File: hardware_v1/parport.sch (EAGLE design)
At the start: 13 parts, among them IC1 74LS541DW, IC2 74LS541DW, IC3 74LS541DW, K1 PIN20X2

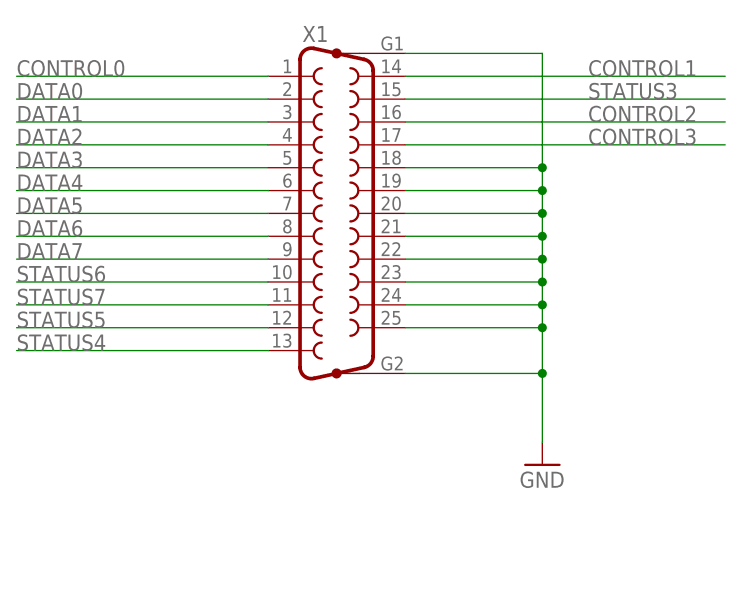
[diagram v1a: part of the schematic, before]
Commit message: hardware_v1: replace DB25 with 2x13 header
It was a mistake to mount a DB25 directly on the adapter.
Use a 26 pin header and then off the shelf header to DB25
adapters can be used to suit the application.
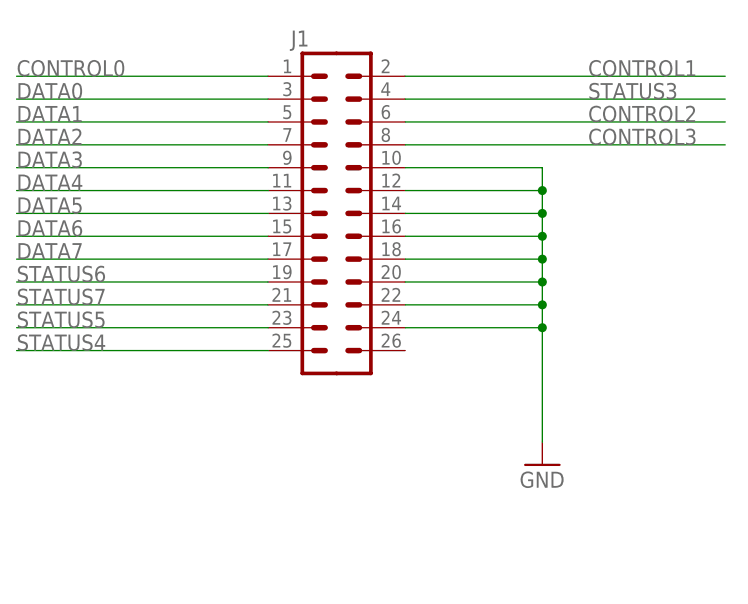
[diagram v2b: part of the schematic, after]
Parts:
- removed X1: (no value), con-subd:F25HP
- added J1: (no value), SparkFun-Connectors:M13X22X13
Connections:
- net CONTROL0: now also J1.1; no longer X1.1
- net CONTROL1: now also J1.2; no longer X1.14
- net CONTROL2: now also J1.6; no longer X1.16
- net CONTROL3: now also J1.8; no longer X1.17
- net DATA0: now also J1.3; no longer X1.2
- net DATA1: now also J1.5; no longer X1.3
- net DATA2: now also J1.7; no longer X1.4
- net DATA3: now also J1.9; no longer X1.5
- net DATA4: now also J1.11; no longer X1.6
- net DATA5: now also J1.13; no longer X1.7
- net DATA6: now also J1.15; no longer X1.8
- net DATA7: now also J1.17; no longer X1.9
- net GND: now also J1.10, J1.12, J1.14, J1.16, J1.18, J1.20, J1.22, J1.24; no longer X1.18, X1.19, X1.20, X1.21, X1.22, X1.23, X1.24, X1.25, X1.G1, X1.G2
- net STATUS3: now also J1.4; no longer X1.15
- net STATUS4: now also J1.25; no longer X1.13
- net STATUS5: now also J1.23; no longer X1.12
- net STATUS6: now also J1.19; no longer X1.10
- net STATUS7: now also J1.21; no longer X1.11
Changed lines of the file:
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@@
 <part name="P+1" library="supply1" deviceset="+5V" device=""/>
 <part name="IC1" library="74xx-us" deviceset="74*541" device="DW" technology="LS"/>
-<part name="X1" library="con-subd" deviceset="F25HP" device=""/>
 <part name="GND1" library="supply1" deviceset="GND" device=""/>
 <part name="IC2" library="74xx-us" deviceset="74*541" device="DW" technology="LS"/>
@@
 <part name="+3V3" library="supply1" deviceset="+3V3" device=""/>
 <part name="P+6" library="supply1" deviceset="+5V" device=""/>
+<part name="J1" library="SparkFun-Connectors" deviceset="M13X2" device="2X13"/>
 </parts>
 <sheets>
@@
 <attribute name="NAME" x="119.38" y="216.535" size="1.778" layer="95"/>
 </instance>
-<instance part="X1" gate="G$1" x="289.56" y="198.12"/>
 <instance part="GND1" gate="1" x="312.42" y="170.18"/>
 <instance part="IC2" gate="A" x="127" y="147.32" smashed="yes">
@@
 <attribute name="VALUE" x="71.12" y="180.34" size="1.778" layer="96" rot="R180"/>
 </instance>
+<instance part="J1" gate="G$1" x="289.56" y="198.12"/>
 </instances>
 <busses>
@@
 </segment>
 <segment>
-<pinref part="X1" gate="G$1" pin="18"/>
 <wire x1="297.18" y1="203.2" x2="312.42" y2="203.2" width="0.1524" layer="91"/>
 <wire x1="312.42" y1="203.2" x2="312.42" y2="200.66" width="0.1524" layer="91"/>
-<pinref part="X1" gate="G$1" pin="19"/>
 <wire x1="312.42" y1="200.66" x2="312.42" y2="198.12" width="0.1524" layer="91"/>
 <wire x1="312.42" y1="198.12" x2="312.42" y2="195.58" width="0.1524" layer="91"/>
@@
 <wire x1="312.42" y1="190.5" x2="312.42" y2="187.96" width="0.1524" layer="91"/>
 <wire x1="312.42" y1="187.96" x2="312.42" y2="185.42" width="0.1524" layer="91"/>
-<wire x1="312.42" y1="185.42" x2="312.42" y2="180.34" width="0.1524" layer="91"/>
-<wire x1="312.42" y1="180.34" x2="312.42" y2="172.72" width="0.1524" layer="91"/>
+<wire x1="312.42" y1="185.42" x2="312.42" y2="172.72" width="0.1524" layer="91"/>
 <wire x1="297.18" y1="200.66" x2="312.42" y2="200.66" width="0.1524" layer="91"/>
 <junction x="312.42" y="200.66"/>
-<pinref part="X1" gate="G$1" pin="20"/>
 <wire x1="297.18" y1="198.12" x2="312.42" y2="198.12" width="0.1524" layer="91"/>
 <junction x="312.42" y="198.12"/>
-<pinref part="X1" gate="G$1" pin="21"/>
 <wire x1="297.18" y1="195.58" x2="312.42" y2="195.58" width="0.1524" layer="91"/>
 <junction x="312.42" y="195.58"/>
-<pinref part="X1" gate="G$1" pin="22"/>
 <wire x1="297.18" y1="193.04" x2="312.42" y2="193.04" width="0.1524" layer="91"/>
 <junction x="312.42" y="193.04"/>
-<pinref part="X1" gate="G$1" pin="23"/>
 <wire x1="297.18" y1="190.5" x2="312.42" y2="190.5" width="0.1524" layer="91"/>
 <junction x="312.42" y="190.5"/>
-<pinref part="X1" gate="G$1" pin="24"/>
 <wire x1="297.18" y1="187.96" x2="312.42" y2="187.96" width="0.1524" layer="91"/>
 <junction x="312.42" y="187.96"/>
-<pinref part="X1" gate="G$1" pin="25"/>
 <wire x1="297.18" y1="185.42" x2="312.42" y2="185.42" width="0.1524" layer="91"/>
 <junction x="312.42" y="185.42"/>
 <pinref part="GND1" gate="1" pin="GND"/>
-<pinref part="X1" gate="G$1" pin="G2"/>
-<wire x1="297.18" y1="180.34" x2="312.42" y2="180.34" width="0.1524" layer="91"/>
-<junction x="312.42" y="180.34"/>
-<pinref part="X1" gate="G$1" pin="G1"/>
-<wire x1="297.18" y1="215.9" x2="312.42" y2="215.9" width="0.1524" layer="91"/>
-<wire x1="312.42" y1="215.9" x2="312.42" y2="203.2" width="0.1524" layer="91"/>
-<junction x="312.42" y="203.2"/>
+<pinref part="J1" gate="G$1" pin="24"/>
+<pinref part="J1" gate="G$1" pin="22"/>
+<pinref part="J1" gate="G$1" pin="20"/>
+<pinref part="J1" gate="G$1" pin="18"/>
+<pinref part="J1" gate="G$1" pin="16"/>
+<pinref part="J1" gate="G$1" pin="14"/>
+<pinref part="J1" gate="G$1" pin="12"/>
+<pinref part="J1" gate="G$1" pin="10"/>
 </segment>
 <segment>
@@
 <net name="DATA0" class="0">
 <segment>
-<pinref part="X1" gate="G$1" pin="2"/>
 <wire x1="281.94" y1="210.82" x2="254" y2="210.82" width="0.1524" layer="91"/>
 <label x="254" y="210.82" size="1.778" layer="95"/>
+<pinref part="J1" gate="G$1" pin="3"/>
 </segment>
 <segment>
@@
 <net name="DATA1" class="0">
 <segment>
-<pinref part="X1" gate="G$1" pin="3"/>
 <wire x1="281.94" y1="208.28" x2="254" y2="208.28" width="0.1524" layer="91"/>
 <label x="254" y="208.28" size="1.778" layer="95"/>
+<pinref part="J1" gate="G$1" pin="5"/>
 </segment>
 <segment>
@@
 <net name="DATA2" class="0">
 <segment>
-<pinref part="X1" gate="G$1" pin="4"/>
 <wire x1="281.94" y1="205.74" x2="254" y2="205.74" width="0.1524" layer="91"/>
 <label x="254" y="205.74" size="1.778" layer="95"/>
+<pinref part="J1" gate="G$1" pin="7"/>
 </segment>
 <segment>
@@
 <net name="DATA3" class="0">
 <segment>
-<pinref part="X1" gate="G$1" pin="5"/>
 <wire x1="281.94" y1="203.2" x2="254" y2="203.2" width="0.1524" layer="91"/>
 <label x="254" y="203.2" size="1.778" layer="95"/>
+<pinref part="J1" gate="G$1" pin="9"/>
 </segment>
 <segment>
@@
 <net name="DATA4" class="0">
 <segment>
-<pinref part="X1" gate="G$1" pin="6"/>
 <wire x1="281.94" y1="200.66" x2="254" y2="200.66" width="0.1524" layer="91"/>
 <label x="254" y="200.66" size="1.778" layer="95"/>
+<pinref part="J1" gate="G$1" pin="11"/>
 </segment>
 <segment>
@@
 <net name="DATA5" class="0">
 <segment>
-<pinref part="X1" gate="G$1" pin="7"/>
 <wire x1="281.94" y1="198.12" x2="254" y2="198.12" width="0.1524" layer="91"/>
 <label x="254" y="198.12" size="1.778" layer="95"/>
+<pinref part="J1" gate="G$1" pin="13"/>
 </segment>
 <segment>
@@
 <net name="DATA6" class="0">
 <segment>
-<pinref part="X1" gate="G$1" pin="8"/>
 <wire x1="281.94" y1="195.58" x2="254" y2="195.58" width="0.1524" layer="91"/>
 <label x="254" y="195.58" size="1.778" layer="95"/>
+<pinref part="J1" gate="G$1" pin="15"/>
 </segment>
 <segment>
@@
 <net name="DATA7" class="0">
 <segment>
-<pinref part="X1" gate="G$1" pin="9"/>
 <wire x1="281.94" y1="193.04" x2="254" y2="193.04" width="0.1524" layer="91"/>
 <label x="254" y="193.04" size="1.778" layer="95"/>
+<pinref part="J1" gate="G$1" pin="17"/>
 </segment>
 <segment>
@@
 <net name="CONTROL0" class="0">
 <segment>
-<pinref part="X1" gate="G$1" pin="1"/>
 <wire x1="281.94" y1="213.36" x2="254" y2="213.36" width="0.1524" layer="91"/>
 <label x="254" y="213.36" size="1.778" layer="95"/>
+<pinref part="J1" gate="G$1" pin="1"/>
 </segment>
 <segment>
@@
 <net name="STATUS6" class="0">
 <segment>
-<pinref part="X1" gate="G$1" pin="10"/>
 <wire x1="281.94" y1="190.5" x2="254" y2="190.5" width="0.1524" layer="91"/>
 <label x="254" y="190.5" size="1.778" layer="95"/>
+<pinref part="J1" gate="G$1" pin="19"/>
 </segment>
 <segment>
@@
 <net name="STATUS5" class="0">
 <segment>
-<pinref part="X1" gate="G$1" pin="12"/>
 <wire x1="281.94" y1="185.42" x2="254" y2="185.42" width="0.1524" layer="91"/>
 <label x="254" y="185.42" size="1.778" layer="95"/>
+<pinref part="J1" gate="G$1" pin="23"/>
 </segment>
 <segment>
@@
 <net name="CONTROL1" class="0">
 <segment>
-<pinref part="X1" gate="G$1" pin="14"/>
 <wire x1="297.18" y1="213.36" x2="332.74" y2="213.36" width="0.1524" layer="91"/>
 <label x="317.5" y="213.36" size="1.778" layer="95"/>
+<pinref part="J1" gate="G$1" pin="2"/>
 </segment>
 <segment>
@@
 <net name="STATUS3" class="0">
 <segment>
-<pinref part="X1" gate="G$1" pin="15"/>
 <wire x1="297.18" y1="210.82" x2="332.74" y2="210.82" width="0.1524" layer="91"/>
 <label x="317.5" y="210.82" size="1.778" layer="95"/>
+<pinref part="J1" gate="G$1" pin="4"/>
 </segment>
 <segment>
@@
 <net name="CONTROL2" class="0">
 <segment>
-<pinref part="X1" gate="G$1" pin="16"/>
 <wire x1="297.18" y1="208.28" x2="332.74" y2="208.28" width="0.1524" layer="91"/>
 <label x="317.5" y="208.28" size="1.778" layer="95"/>
+<pinref part="J1" gate="G$1" pin="6"/>
 </segment>
 <segment>
@@
 <net name="CONTROL3" class="0">
 <segment>
-<pinref part="X1" gate="G$1" pin="17"/>
 <wire x1="297.18" y1="205.74" x2="332.74" y2="205.74" width="0.1524" layer="91"/>
 <label x="317.5" y="205.74" size="1.778" layer="95"/>
+<pinref part="J1" gate="G$1" pin="8"/>
 </segment>
 <segment>
@@
 <net name="STATUS4" class="0">
 <segment>
-<pinref part="X1" gate="G$1" pin="13"/>
 <wire x1="281.94" y1="182.88" x2="254" y2="182.88" width="0.1524" layer="91"/>
 <label x="254" y="182.88" size="1.778" layer="95"/>
+<pinref part="J1" gate="G$1" pin="25"/>
 </segment>
 <segment>
@@
 <net name="STATUS7" class="0">
 <segment>
-<pinref part="X1" gate="G$1" pin="11"/>
 <wire x1="281.94" y1="187.96" x2="254" y2="187.96" width="0.1524" layer="91"/>
 <label x="254" y="187.96" size="1.778" layer="95"/>
-</segment>
-<segment>
+<pinref part="J1" gate="G$1" pin="21"/>
+</segment>
+<segment>

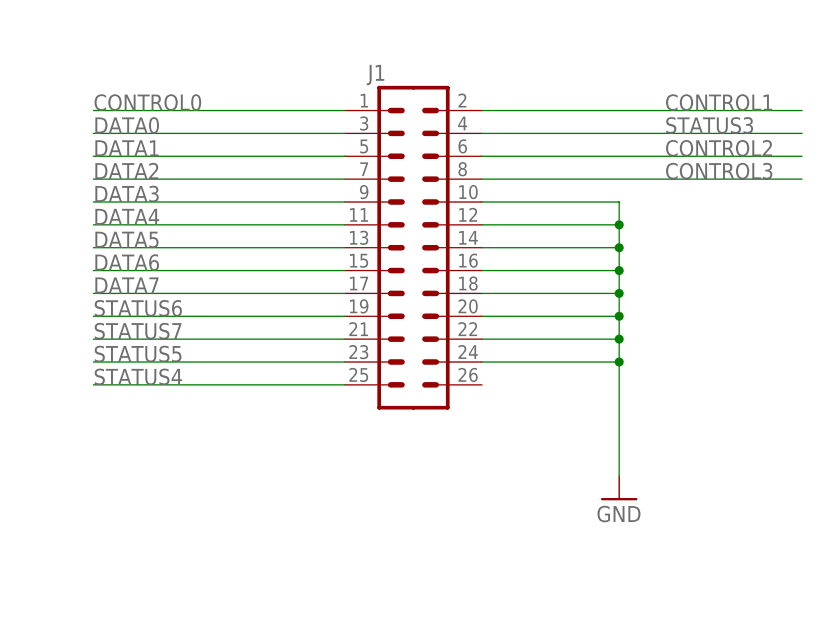
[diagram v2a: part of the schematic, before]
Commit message: hardware_v1: include DB-25 pin numbering on schematic
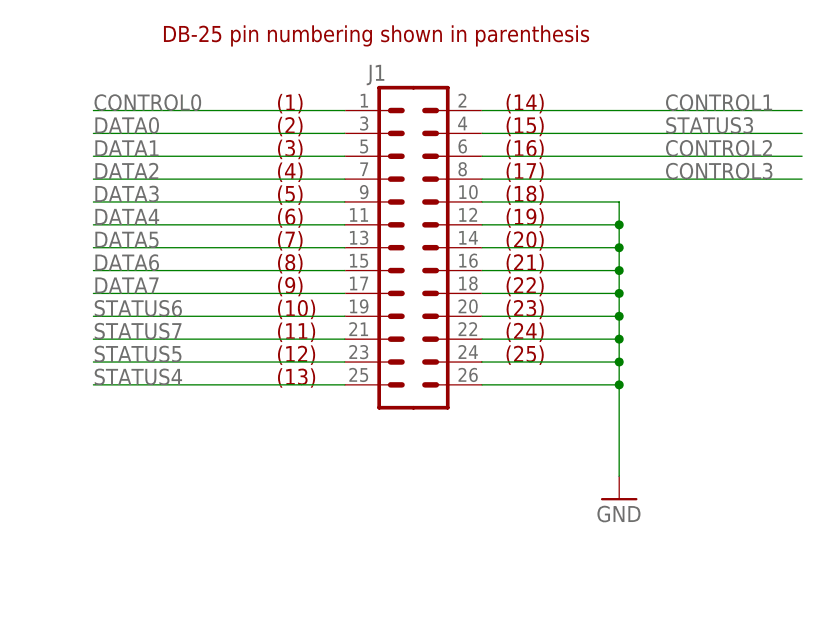
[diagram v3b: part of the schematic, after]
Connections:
- net GND: now also J1.26
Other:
- note added: "(1)"
- note added: "(10)"
- note added: "(11)"
- note added: "(12)"
- note added: "(13)"
- note added: "(14)"
- note added: "(15)"
- note added: "(16)"
- note added: "(17)"
- note added: "(18)"
- note added: "(19)"
- note added: "(2)"
- note added: "(20)"
- note added: "(21)"
- note added: "(22)"
- note added: "(23)"
- note added: "(24)"
- note added: "(25)"
- note added: "(3)"
- note added: "(4)"
- note added: "(5)"
- note added: "(6)"
- note added: "(7)"
- note added: "(8)"
- note added: "(9)"
- note added: "DB-25 pin numbering shown in parenthesis"
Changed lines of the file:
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@@
 <text x="121.92" y="73.66" size="1.778" layer="91">VCC=5V</text>
 <text x="121.92" y="127" size="1.778" layer="91">VCC=3V3</text>
+<text x="274.32" y="213.36" size="1.778" layer="94">(1)</text>
+<text x="274.32" y="210.82" size="1.778" layer="94">(2)</text>
+<text x="274.32" y="208.28" size="1.778" layer="94">(3)</text>
+<text x="274.32" y="205.74" size="1.778" layer="94">(4)</text>
+<text x="274.32" y="203.2" size="1.778" layer="94">(5)</text>
+<text x="274.32" y="200.66" size="1.778" layer="94">(6)</text>
+<text x="274.32" y="198.12" size="1.778" layer="94">(7)</text>
+<text x="274.32" y="195.58" size="1.778" layer="94">(8)</text>
+<text x="274.32" y="193.04" size="1.778" layer="94">(9)</text>
+<text x="274.32" y="190.5" size="1.778" layer="94">(10)</text>
+<text x="274.32" y="187.96" size="1.778" layer="94">(11)</text>
+<text x="274.32" y="185.42" size="1.778" layer="94">(12)</text>
+<text x="274.32" y="182.88" size="1.778" layer="94">(13)</text>
+<text x="299.72" y="213.36" size="1.778" layer="94">(14)</text>
+<text x="299.72" y="210.82" size="1.778" layer="94">(15)</text>
+<text x="299.72" y="205.74" size="1.778" layer="94">(17)</text>
+<text x="299.72" y="203.2" size="1.778" layer="94">(18)</text>
+<text x="299.72" y="200.66" size="1.778" layer="94">(19)</text>
+<text x="299.72" y="198.12" size="1.778" layer="94">(20)</text>
+<text x="299.72" y="195.58" size="1.778" layer="94">(21)</text>
+<text x="299.72" y="193.04" size="1.778" layer="94">(22)</text>
+<text x="299.72" y="190.5" size="1.778" layer="94">(23)</text>
+<text x="299.72" y="187.96" size="1.778" layer="94">(24)</text>
+<text x="299.72" y="185.42" size="1.778" layer="94">(25)</text>
+<text x="299.72" y="208.28" size="1.778" layer="94">(16)</text>
+<text x="261.62" y="220.98" size="1.778" layer="94">DB-25 pin numbering shown in parenthesis</text>
 </plain>
 <instances>
@@
 <wire x1="312.42" y1="190.5" x2="312.42" y2="187.96" width="0.1524" layer="91"/>
 <wire x1="312.42" y1="187.96" x2="312.42" y2="185.42" width="0.1524" layer="91"/>
-<wire x1="312.42" y1="185.42" x2="312.42" y2="172.72" width="0.1524" layer="91"/>
+<wire x1="312.42" y1="185.42" x2="312.42" y2="182.88" width="0.1524" layer="91"/>
+<wire x1="312.42" y1="182.88" x2="312.42" y2="172.72" width="0.1524" layer="91"/>
 <wire x1="297.18" y1="200.66" x2="312.42" y2="200.66" width="0.1524" layer="91"/>
 <junction x="312.42" y="200.66"/>
@@
 <pinref part="J1" gate="G$1" pin="12"/>
 <pinref part="J1" gate="G$1" pin="10"/>
+<pinref part="J1" gate="G$1" pin="26"/>
+<wire x1="297.18" y1="182.88" x2="312.42" y2="182.88" width="0.1524" layer="91"/>
+<junction x="312.42" y="182.88"/>
 </segment>
 <segment>
